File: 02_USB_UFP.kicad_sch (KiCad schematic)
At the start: 27 parts, among them J1 USB_C_Receptacle, U5 TVS2200DRVx, U6 PI3USB302-Ax, U7 TUSB522Px

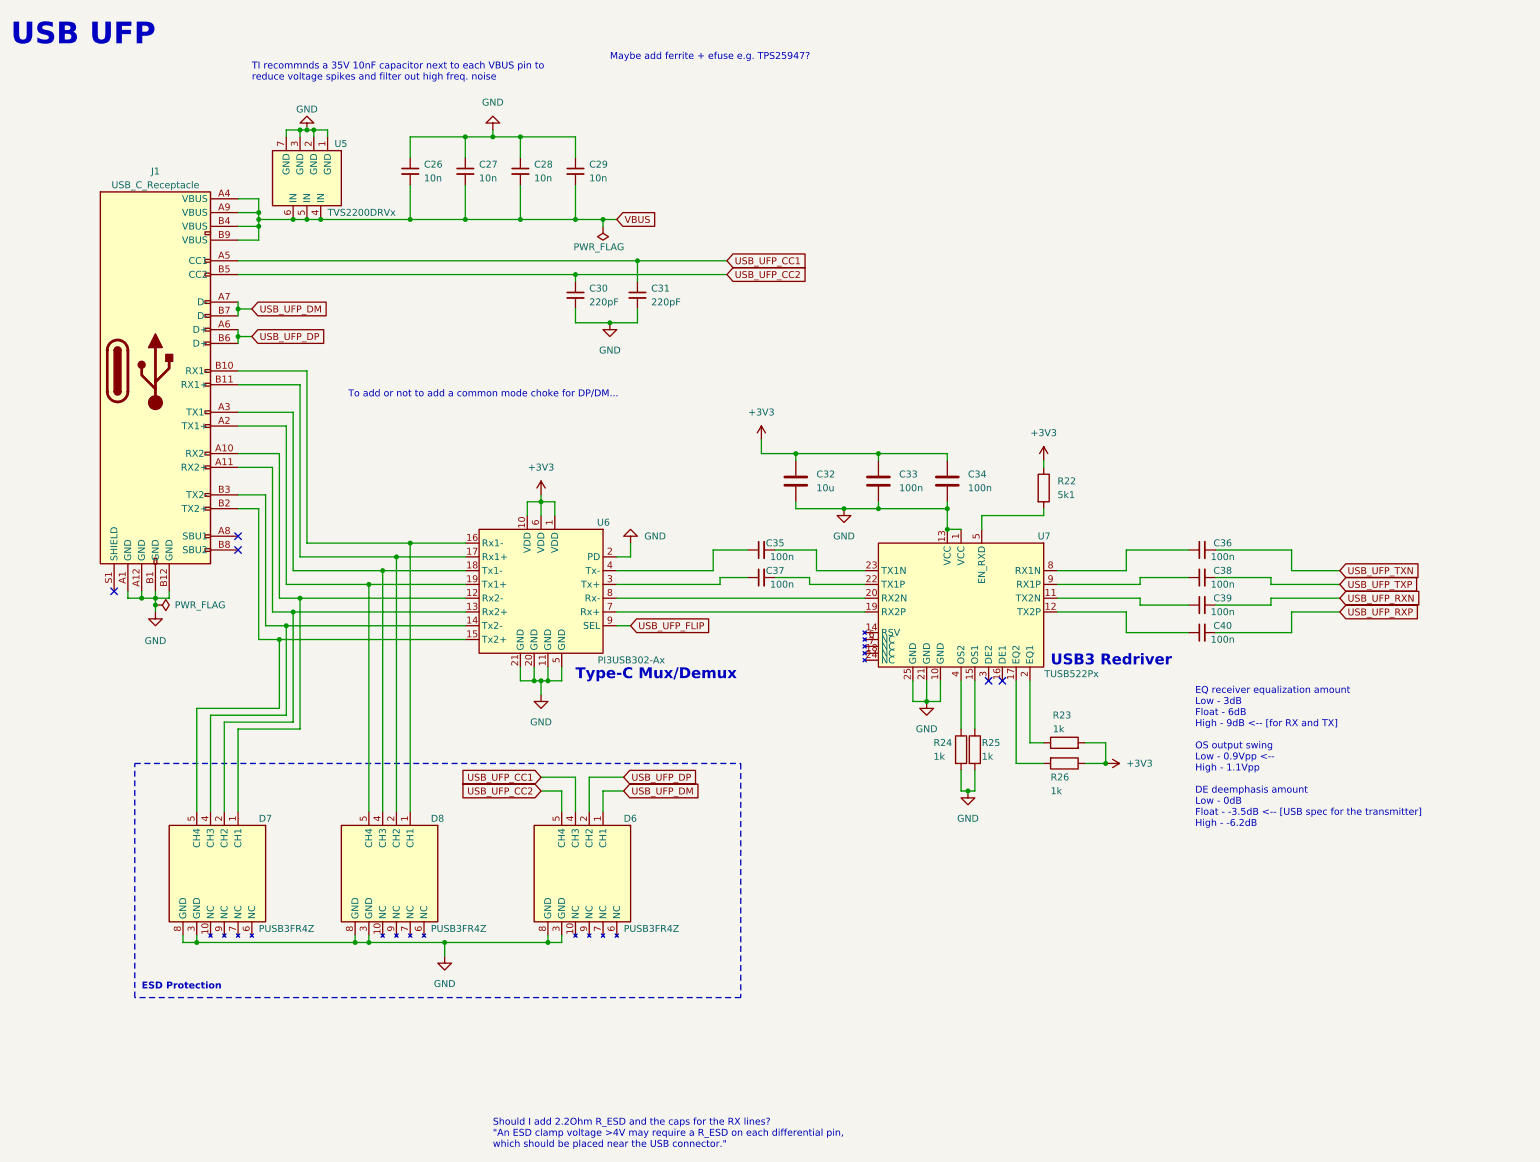
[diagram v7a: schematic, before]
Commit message: fix symbols, route UFP DPs and voltage regs
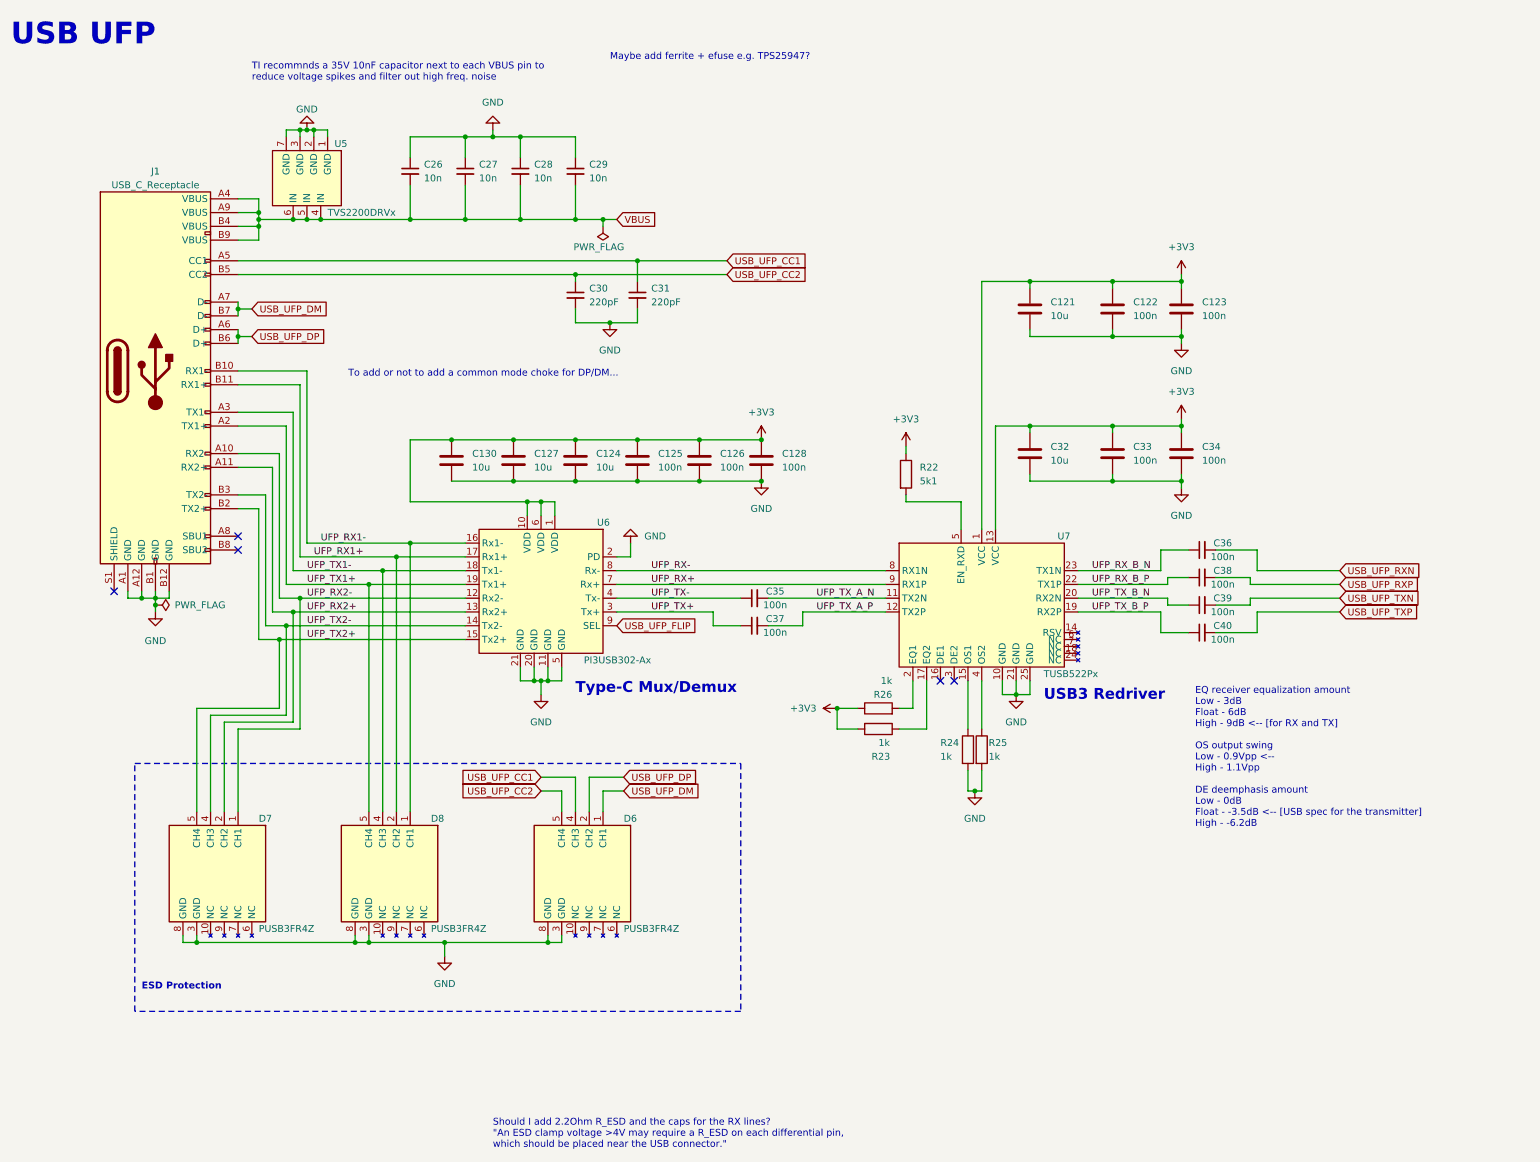
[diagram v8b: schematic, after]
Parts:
- added C121, C124, C127, C130: 10u, Capacitor_SMD:C_0603_1608Metric, symbol Device:C
- added C122, C123, C125, C126, C128: 100n, Capacitor_SMD:C_0603_1608Metric, symbol Device:C
- J1: footprint CakeUSB:USB_C_Receptacle_GT-USB-7052 -> CakeUSB:USB_C_Receptacle_GT-USB-7028x
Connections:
- net +3V3: now also U7.1 (VCC), U7.13 (VCC), C121.1, C122.1, C123.1, C124.1, C125.1, C126.1, C127.1, C128.1, C130.1
- net GND: now also C121.2, C122.2, C123.2, C124.2, C125.2, C126.2, C127.2, C128.2, C130.2; no longer U7.1 (VCC), U7.13 (VCC)
- net USB_UFP_RXN: now also C36.2; no longer C39.2
- net USB_UFP_RXP: now also C38.2; no longer C40.2
- net USB_UFP_TXN: now also C39.2; no longer C36.2
- net USB_UFP_TXP: now also C40.2; no longer C38.2
- net UFP_RX+: now reaches U7.9 (RX1P)
- net UFP_RX+: now also U6.7 (Rx+); no longer C38.1
- net UFP_RX-: now reaches U7.8 (RX1N)
- net UFP_RX-: now also U6.8 (Rx-); no longer C36.1
- net UFP_TX_A_N: now reaches U7.11 (TX2N)
- net UFP_TX_A_N: now also C35.2; no longer C39.1
- net at R26.2: now also U7.2 (EQ1); no longer U7.17 (EQ2)
- net UFP_RX1-: now reaches D8.1 (CH1), J1.B10 (RX1-), U6.16 (Rx1-)
- net UFP_RX1+: now reaches D8.2 (CH2), J1.B11 (RX1+), U6.17 (Rx1+)
- net UFP_TX1-: now reaches D8.4 (CH3), J1.A3 (TX1-), U6.18 (Tx1-)
- net UFP_TX1+: now reaches D8.5 (CH4), J1.A2 (TX1+), U6.19 (Tx1+)
- net at R24.1: now also U7.15 (OS1); no longer U7.4 (OS2)
- net UFP_TX+: now reaches C37.1, U6.3 (Tx+)
- net UFP_RX_B_P: now reaches U7.22 (TX1P)
- net UFP_RX_B_P: now also C38.1; no longer C37.2
- net UFP_TX-: now reaches C35.1, U6.4 (Tx-)
- net UFP_RX_B_N: now reaches U7.23 (TX1N)
- net UFP_RX_B_N: now also C36.1; no longer C35.2
- net UFP_RX2-: now reaches D7.1 (CH1), J1.A10 (RX2-), U6.12 (Rx2-)
- net UFP_RX2+: now reaches D7.2 (CH2), J1.A11 (RX2+), U6.13 (Rx2+)
- net UFP_TX2-: now reaches D7.4 (CH3), J1.B3 (TX2-), U6.14 (Tx2-)
- net UFP_TX2+: now reaches D7.5 (CH4), J1.B2 (TX2+), U6.15 (Tx2+)
- net UFP_TX_B_P: now reaches U7.19 (RX2P)
- net UFP_TX_B_P: now also C40.1; no longer U6.7 (Rx+)
- net UFP_TX_B_N: now reaches U7.20 (RX2N)
- net UFP_TX_B_N: now also C39.1; no longer U6.8 (Rx-)
- net UFP_TX_A_P: now reaches U7.12 (TX2P)
- net UFP_TX_A_P: now also C37.2; no longer C40.1
- net at R25.1: now also U7.4 (OS2); no longer U7.15 (OS1)
- net at R23.1: now also U7.17 (EQ2); no longer U7.2 (EQ1)
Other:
- moved on the sheet: C34, C35, C37, R22, R24, R25
